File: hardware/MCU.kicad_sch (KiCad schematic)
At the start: 1 part, among them U2 MAX-M10S

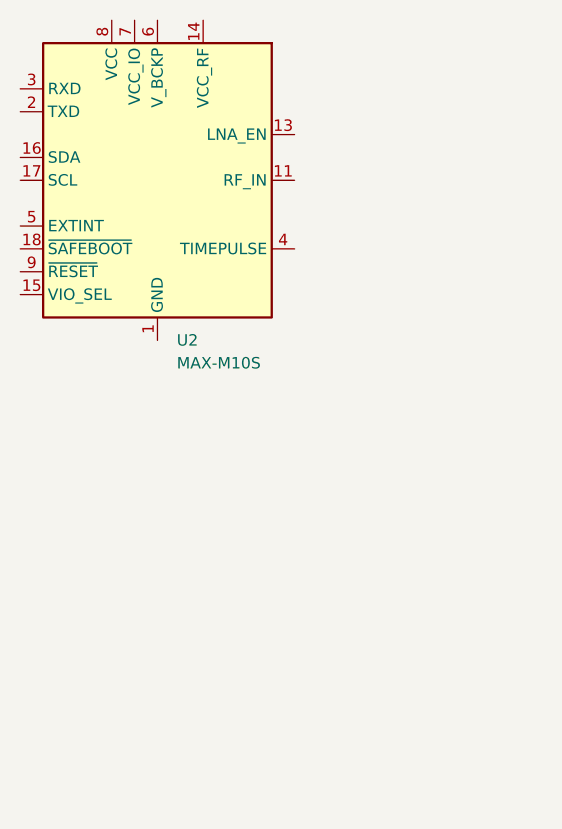
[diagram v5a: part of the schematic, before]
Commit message: Created GPS sheet
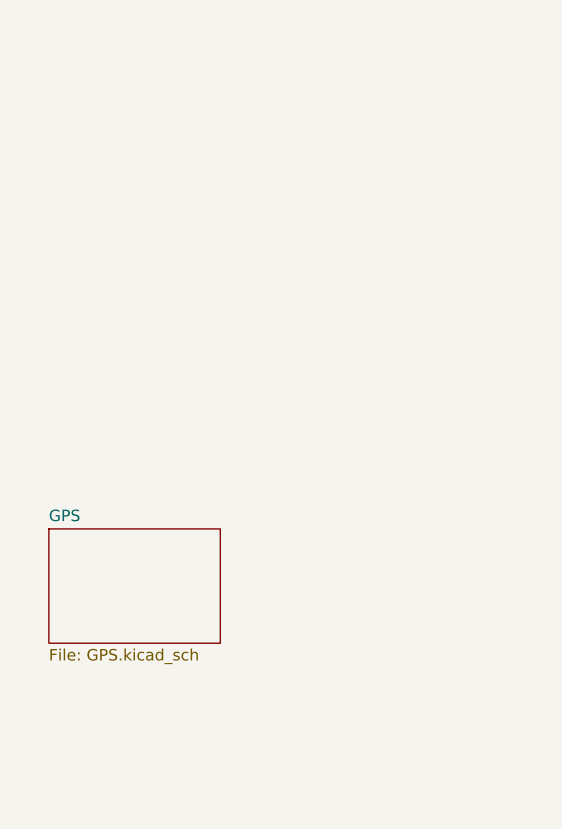
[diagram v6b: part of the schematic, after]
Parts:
- removed U2: MAX-M10S, RF_GPS:ublox_MAX, symbol RF_GPS:MAX-M10S
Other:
- added sheet GPS (GPS.kicad_sch)
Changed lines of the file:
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@@
-		)
-	)
-	(symbol
-		(lib_id "RF_GPS:MAX-M10S")
-		(at 54.61 33.02 0)
-		(unit 1)
-		(body_style 1)
-		(exclude_from_sim no)
-		(in_bom yes)
-		(on_board yes)
-		(in_pos_files yes)
-		(dnp no)
-		(fields_autoplaced yes)
-		(property "Reference" "U2"
-			(at 56.7533 50.8 0)
-			(show_name no)
-			(do_not_autoplace no)
-			(effects
-				(font
-					(size 1.27 1.27)
-				)
-				(justify left)
-			)
-		)
-		(property "Value" "MAX-M10S"
-			(at 56.7533 53.34 0)
-			(show_name no)
-			(do_not_autoplace no)
-			(effects
-				(font
-					(size 1.27 1.27)
-				)
-				(justify left)
-			)
-		)
-		(property "Footprint" "RF_GPS:ublox_MAX"
-			(at 64.77 49.53 0)
-			(hide yes)
-			(show_name no)
-			(do_not_autoplace no)
-			(effects
-				(font
-					(size 1.27 1.27)
-				)
-			)
-		)
-		(property "Datasheet" "https://content.u-blox.com/sites/default/files/MAX-M10S_DataSheet_UBX-20035208.pdf"
-			(at 54.61 33.02 0)
-			(hide yes)
-			(show_name no)
-			(do_not_autoplace no)
-			(effects
-				(font
-					(size 1.27 1.27)
-				)
-			)
-		)
-		(property "Description" "GNSS Module MAX M10, VCC 1.65V to 3.6V"
-			(at 54.61 33.02 0)
-			(hide yes)
-			(show_name no)
-			(do_not_autoplace no)
-			(effects
-				(font
-					(size 1.27 1.27)
-				)
-			)
-		)
-		(pin "8"
-		)
-		(pin "7"
-		)
-		(pin "6"
-		)
-		(pin "5"
-		)
-		(pin "4"
-		)
-		(pin "11"
-		)
-		(pin "10"
-		)
-		(pin "9"
-		)
-		(pin "1"
-		)
-		(pin "2"
-		)
-		(pin "3"
-		)
-		(pin "12"
-		)
-		(pin "13"
-		)
-		(pin "14"
-		)
-		(pin "15"
-		)
-		(pin "16"
-		)
-		(pin "17"
-		)
-		(pin "18"
-		)
-		(instances
-			(project "hardware"
-				(path "/a19f636f-b28d-4c43-b96a-b02383edd3eb/66e2f96f-c2f9-49fe-949d-95863aff4e55"
-					(reference "U2")
-					(unit 1)
-				)
-			)
 		)
 	)
@@
 				)
 			)
+		)
+	)
+	(sheet
+		(at 42.545 71.755)
+		(size 19.05 12.7)
+		(exclude_from_sim no)
+		(in_bom yes)
+		(on_board yes)
+		(dnp no)
+		(fields_autoplaced yes)
+		(stroke
+			(width 0.1524)
+			(type solid)
+		)
+		(fill
+			(color 0 0 0 0)
+		)
+		(property "Sheetname" "GPS"
+			(at 42.545 71.0434 0)
+			(show_name no)
+			(do_not_autoplace no)
+			(effects
+				(font
+					(size 1.27 1.27)
+				)
+				(justify left bottom)
+			)
+		)
+		(property "Sheetfile" "GPS.kicad_sch"
+			(at 42.545 85.0396 0)
+			(show_name no)
+			(do_not_autoplace no)
+			(effects
+				(font
+					(size 1.27 1.27)
+				)
+				(justify left top)
+			)
+		)
+		(instances
+			(project "hardware"
+				(path "/a19f636f-b28d-4c43-b96a-b02383edd3eb/66e2f96f-c2f9-49fe-949d-95863aff4e55"
+					(page "6")
+				)
+			)

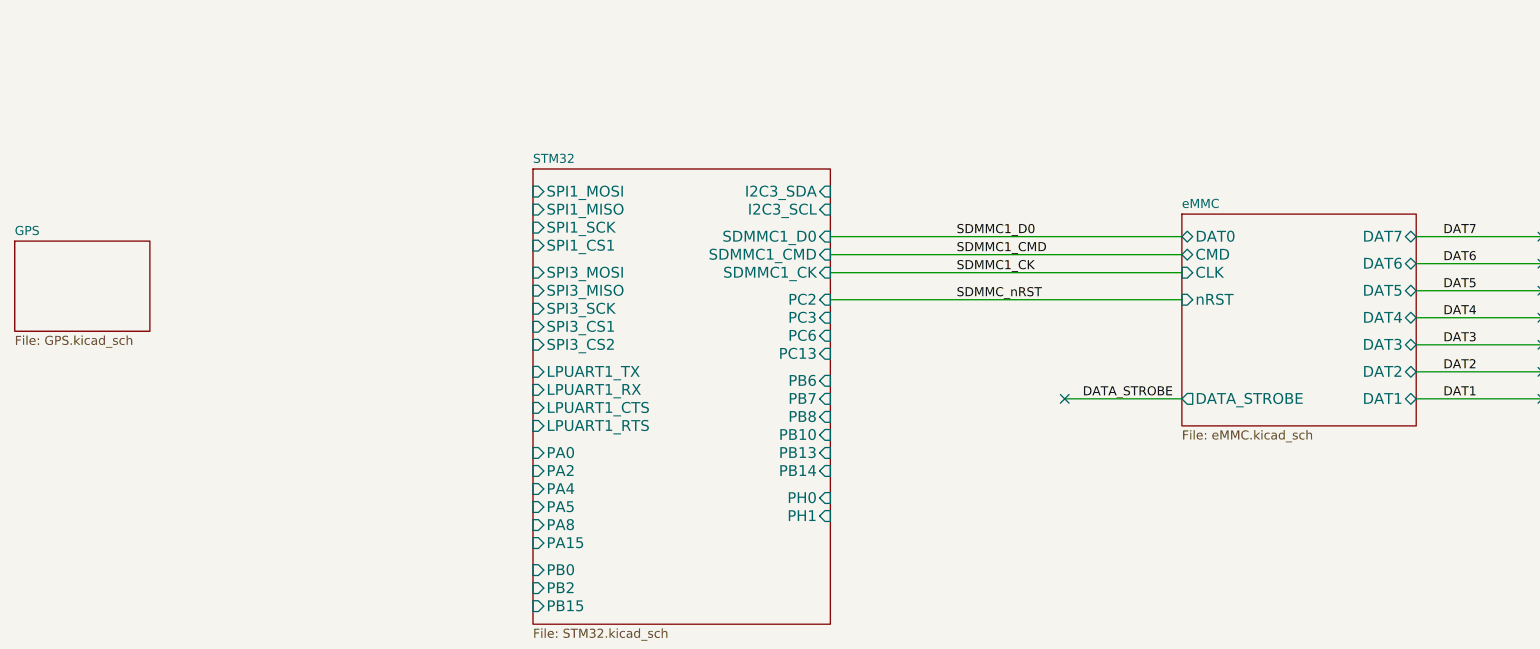
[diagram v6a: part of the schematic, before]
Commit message: Added PPG schematic page
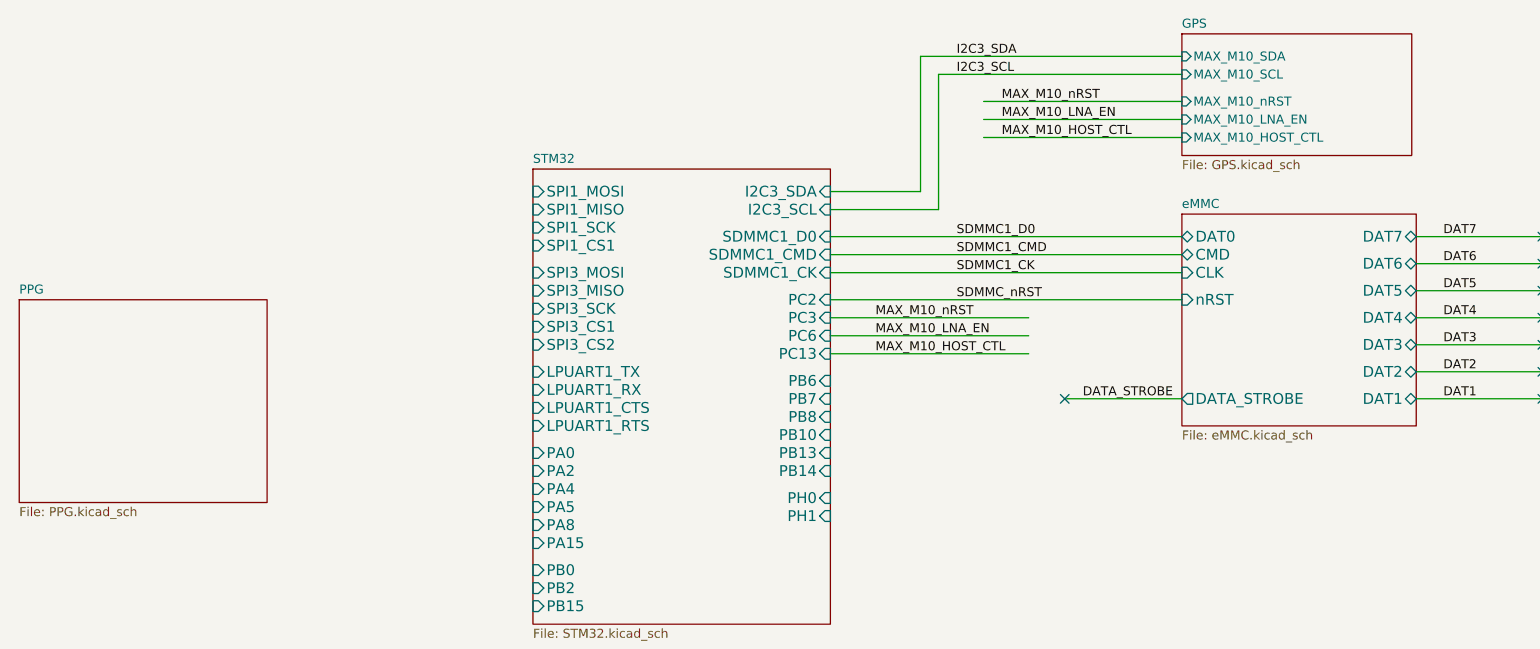
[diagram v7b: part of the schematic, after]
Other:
- added sheet PPG (PPG.kicad_sch)
- sheet GPS ports: added MAX_M10_HOST_CTL, MAX_M10_LNA_EN, MAX_M10_SCL, MAX_M10_SDA, MAX_M10_nRST; removed none

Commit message: Added display block (barely) and freaked out about PPG stuff
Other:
- added sheet User Interface (User_Interface.kicad_sch)
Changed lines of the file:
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@@
 	)
 	(sheet
-		(at 43.18 80.01)
+		(at 32.385 26.035)
+		(size 34.29 25.4)
+		(exclude_from_sim no)
+		(in_bom yes)
+		(on_board yes)
+		(dnp no)
+		(fields_autoplaced yes)
+		(stroke
+			(width 0.1524)
+			(type solid)
+		)
+		(fill
+			(color 0 0 0 0)
+		)
+		(property "Sheetname" "User Interface"
+			(at 32.385 25.3234 0)
+			(show_name no)
+			(do_not_autoplace no)
+			(effects
+				(font
+					(size 1.27 1.27)
+				)
+				(justify left bottom)
+			)
+		)
+		(property "Sheetfile" "User_Interface.kicad_sch"
+			(at 32.385 52.0196 0)
+			(show_name no)
+			(do_not_autoplace no)
+			(effects
+				(font
+					(size 1.27 1.27)
+				)
+				(justify left top)
+			)
+		)
+		(instances
+			(project "hardware"
+				(path "/a19f636f-b28d-4c43-b96a-b02383edd3eb/66e2f96f-c2f9-49fe-949d-95863aff4e55"
+					(page "8")
+				)
+			)
+		)
+	)
+	(sheet
+		(at 31.75 65.405)
 		(size 34.925 28.575)
 		(exclude_from_sim no)
@@
 		)
 		(property "Sheetname" "PPG"
-			(at 43.18 79.2984 0)
+			(at 31.75 64.6934 0)
 			(show_name no)
 			(do_not_autoplace no)
@@
 		)
 		(property "Sheetfile" "PPG.kicad_sch"
-			(at 43.18 109.1696 0)
+			(at 31.75 94.5646 0)
 			(show_name no)
 			(do_not_autoplace no)
